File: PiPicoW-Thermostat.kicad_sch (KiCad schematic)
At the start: 4 parts

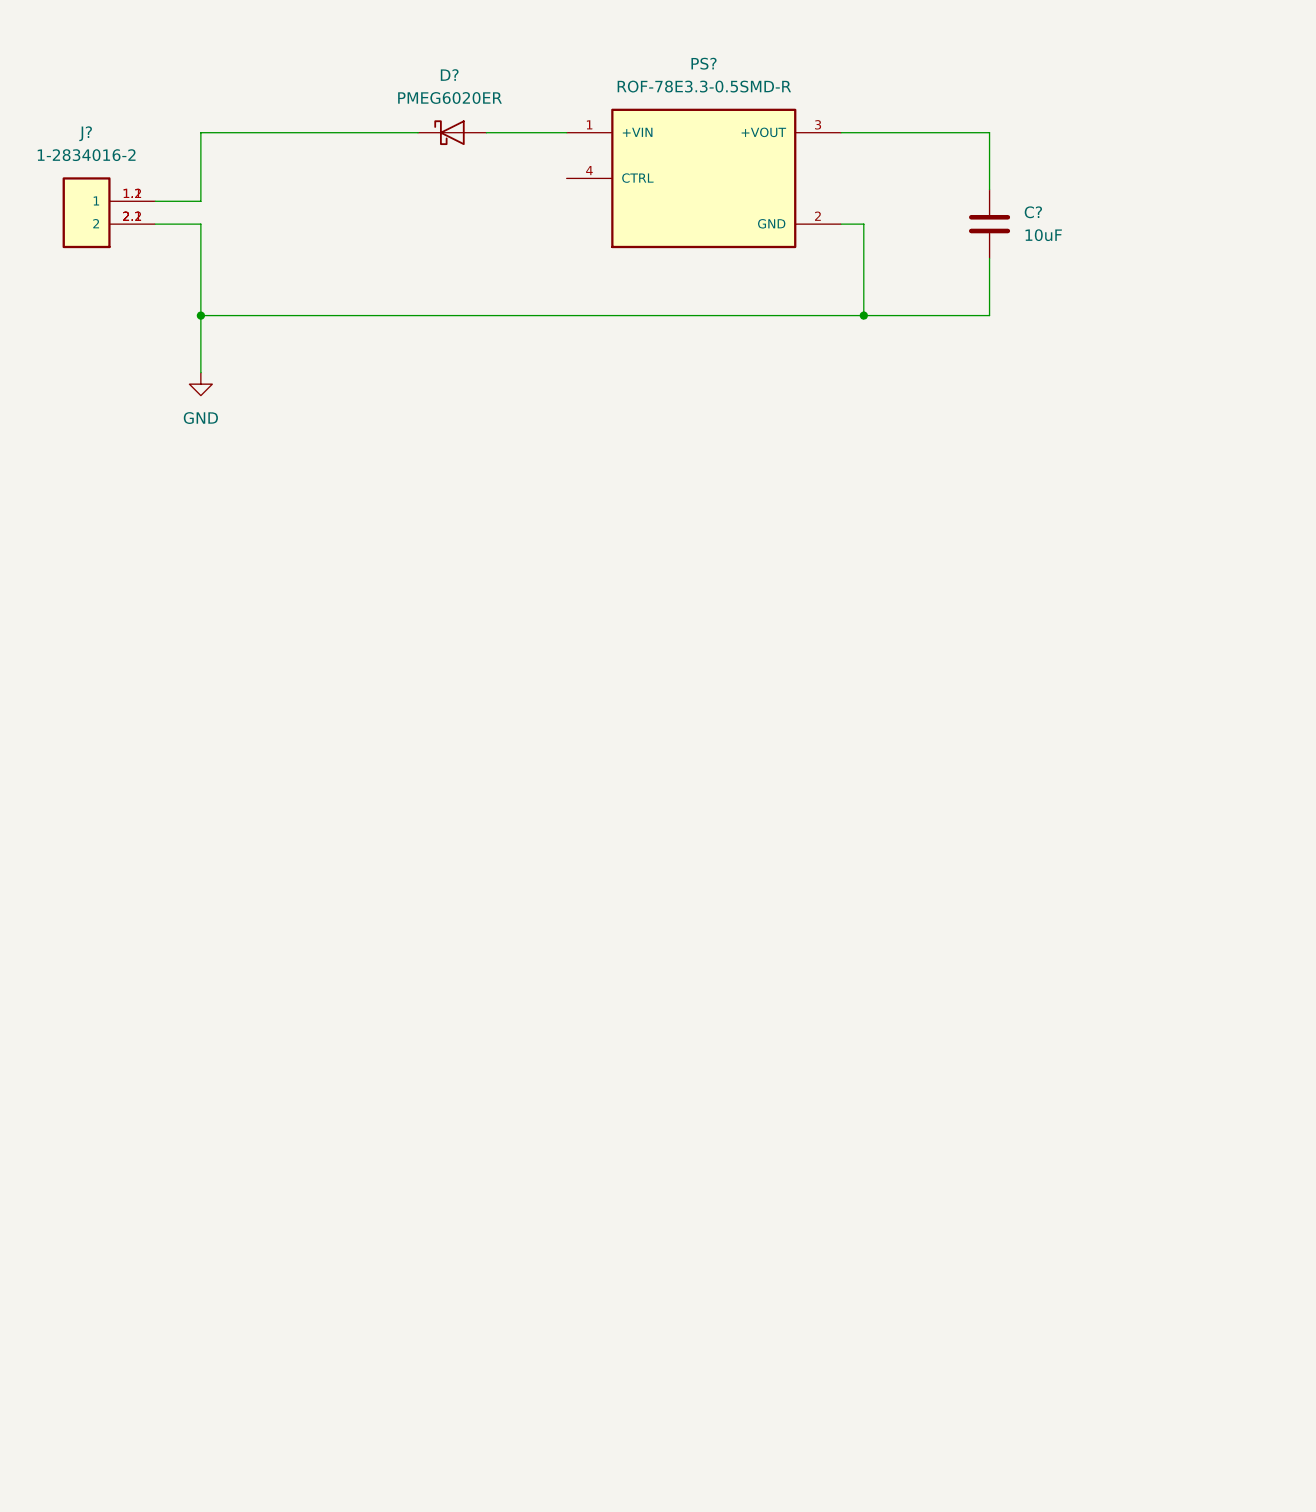
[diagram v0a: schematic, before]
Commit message: Added PicoW
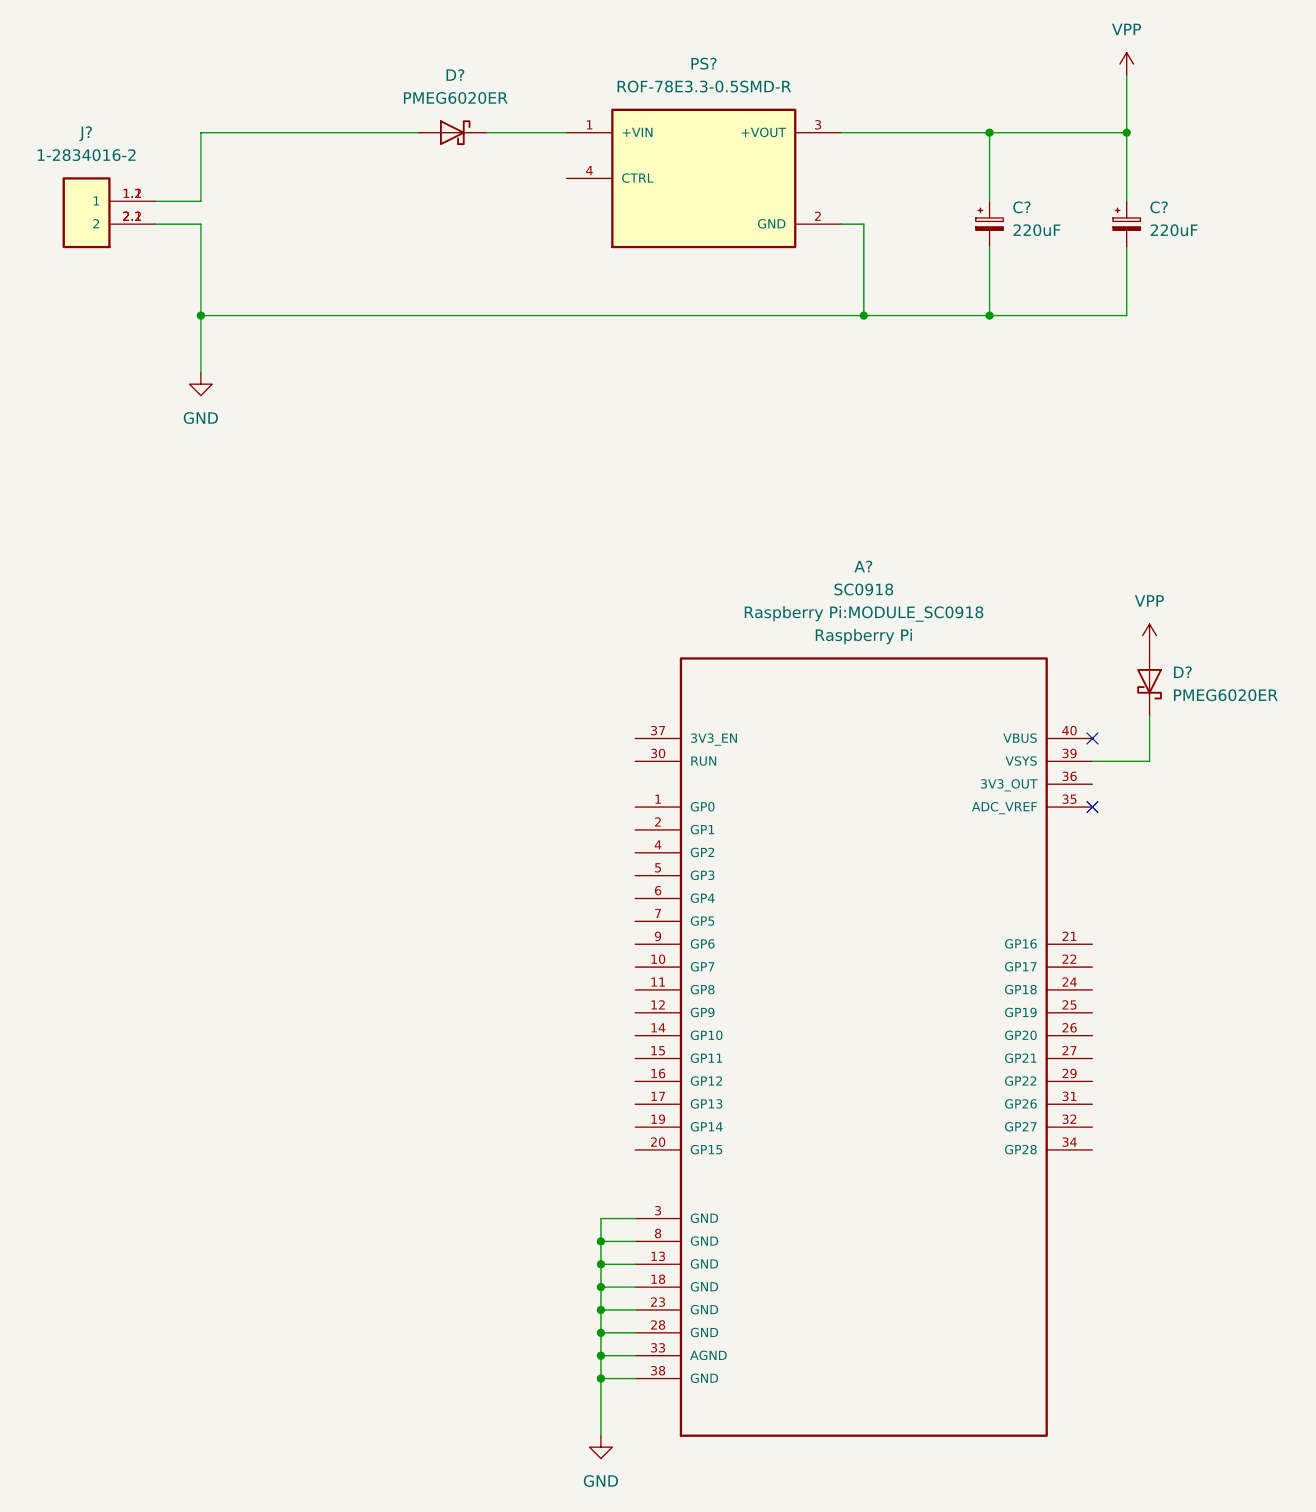
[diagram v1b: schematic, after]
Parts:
- removed C?: 10uF, Capacitor_SMD:C_0805_2012Metric_Pad1.18x1.45mm_HandSolder, symbol Device:C
- added A?: SC0918, Raspberry Pi:MODULE_SC0918, symbol _PicoW:SC0918
- added C? (x2): 220uF, Capacitor_THT:CP_Radial_Tantal_D5.0mm_P5.00mm, symbol Device:C_Polarized_Small
- added D?: PMEG6020ER, Diode_SMD:Nexperia_CFP3_SOD-123W, symbol Diode:PMEG6020ER
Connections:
- net GND: now also A?.13 (GND), A?.18 (GND), A?.23 (GND), A?.28 (GND), A?.3 (GND), A?.33 (AGND), A?.38 (GND), A?.8 (GND), C?.2, C?.2
- net VPP: now reaches PS?.3 (+VOUT)
- net VPP: now also C?.1, C?.1, D?.2 (A)
- net at PS?.1 (+VIN): now also D?.1 (K); no longer D?.2 (A)
- net at J?.1.1 (1), J?.1.2 (1): now also D?.2 (A); no longer D?.1 (K)
- new net: A?.39 (VSYS), D?.1 (K)
- no-connect marks 0 -> 2
